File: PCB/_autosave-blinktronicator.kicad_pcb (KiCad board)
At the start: 2 copper layers, 23.8 x 23.8 mm, 37 parts, among them P3 RST, P4 SCK, P5 MISO, P6 MOSI, SW2 SW_PUSH, SW3 SW_PUSH, U1 ATTINY85-S, U3 74HC595, U4 74HC595

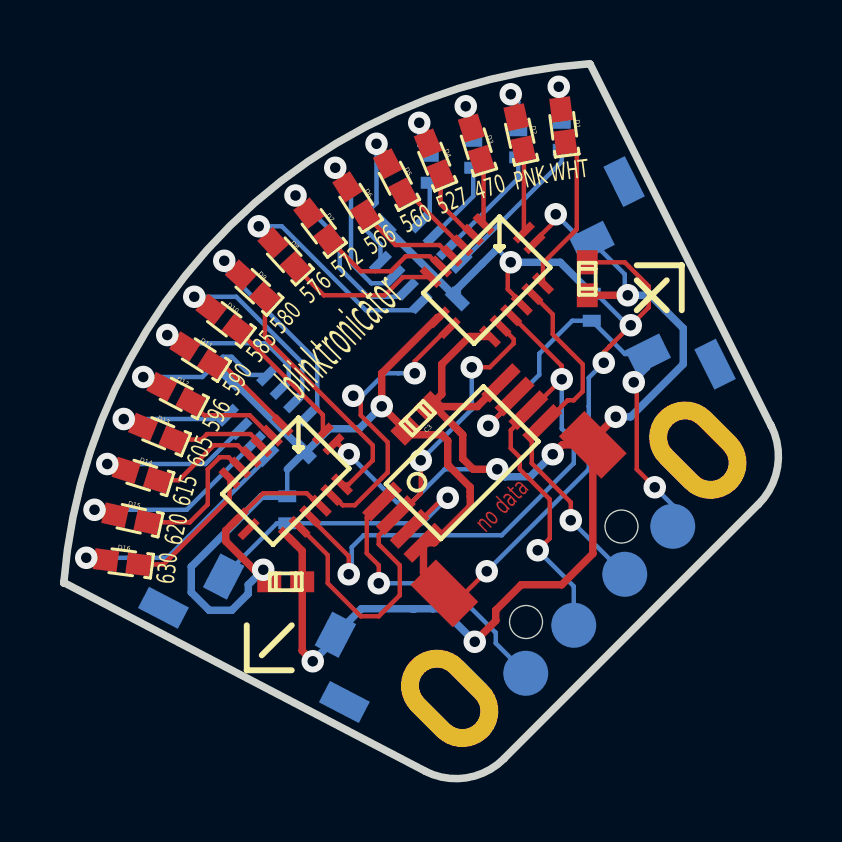
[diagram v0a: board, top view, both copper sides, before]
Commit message: Several minor PCB updates (slots for USB connector, changed silkscreen, etc).
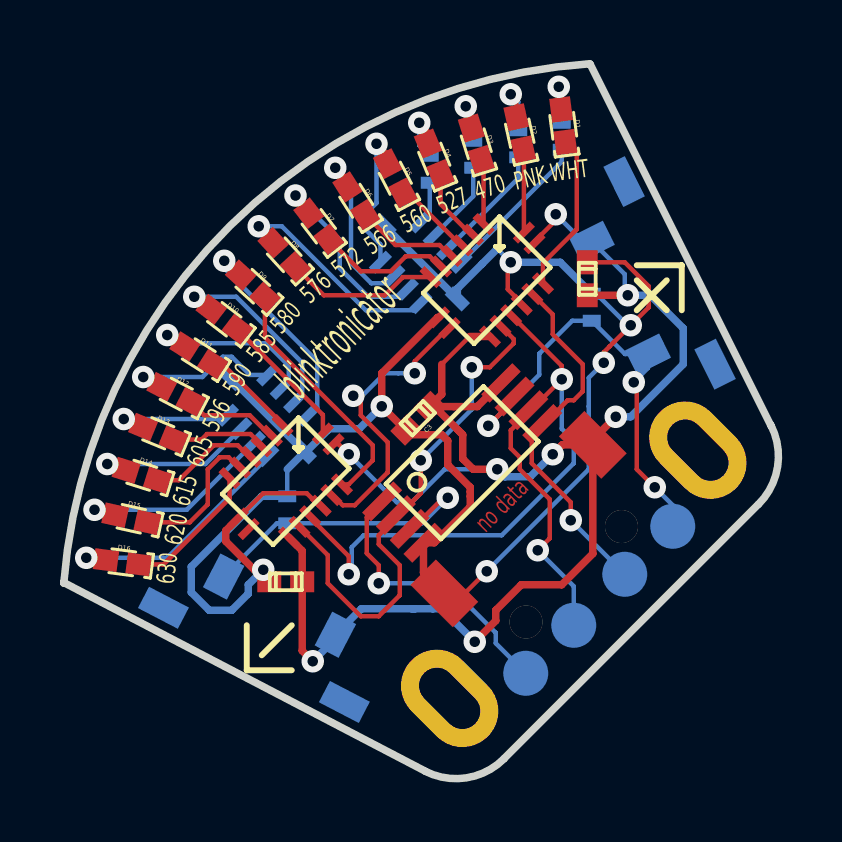
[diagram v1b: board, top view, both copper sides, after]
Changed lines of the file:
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@@
       (net 17 GND)
     )
-    (pad "" np_thru_hole circle (at 2.25 0 45) (size 1.1 1.1) (drill 1.1)
+    (pad "" thru_hole circle (at 2.25 0 45) (size 1.1 1.1) (drill 1.1)
       (layers *.Cu)
     )
-    (pad "" np_thru_hole circle (at -2.25 0 45) (size 1.1 1.1) (drill 1.1)
+    (pad "" thru_hole circle (at -2.25 0 45) (size 1.1 1.1) (drill 1.1)
       (layers *.Cu)
     )
@@
   (segment (start 178 36.3) (end 177.587947 36.712053) (width 0.25) (layer F.Cu) (net 45))
   (segment (start 178 35.3) (end 178 36.3) (width 0.25) (layer F.Cu) (net 45))
-  (segment (start 178.926167 34.373833) (end 178 35.3) (width 0.25) (layer F.Cu) (net 45))
+  (segment (start 178.926167 34.373833) (end 178 35.3) (width 0.15) (layer F.Cu) (net 45))
   (segment (start 181.09099 31.262563) (end 181.09099 31.20901) (width 0.15) (layer F.Cu) (net 45))
   (segment (start 182.699906 31.199906) (end 183.00229 31.199906) (width 0.15) (layer B.Cu) (net 45))
